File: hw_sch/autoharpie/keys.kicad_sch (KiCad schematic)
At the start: 1 part, among them U5 STM32F030R8Tx

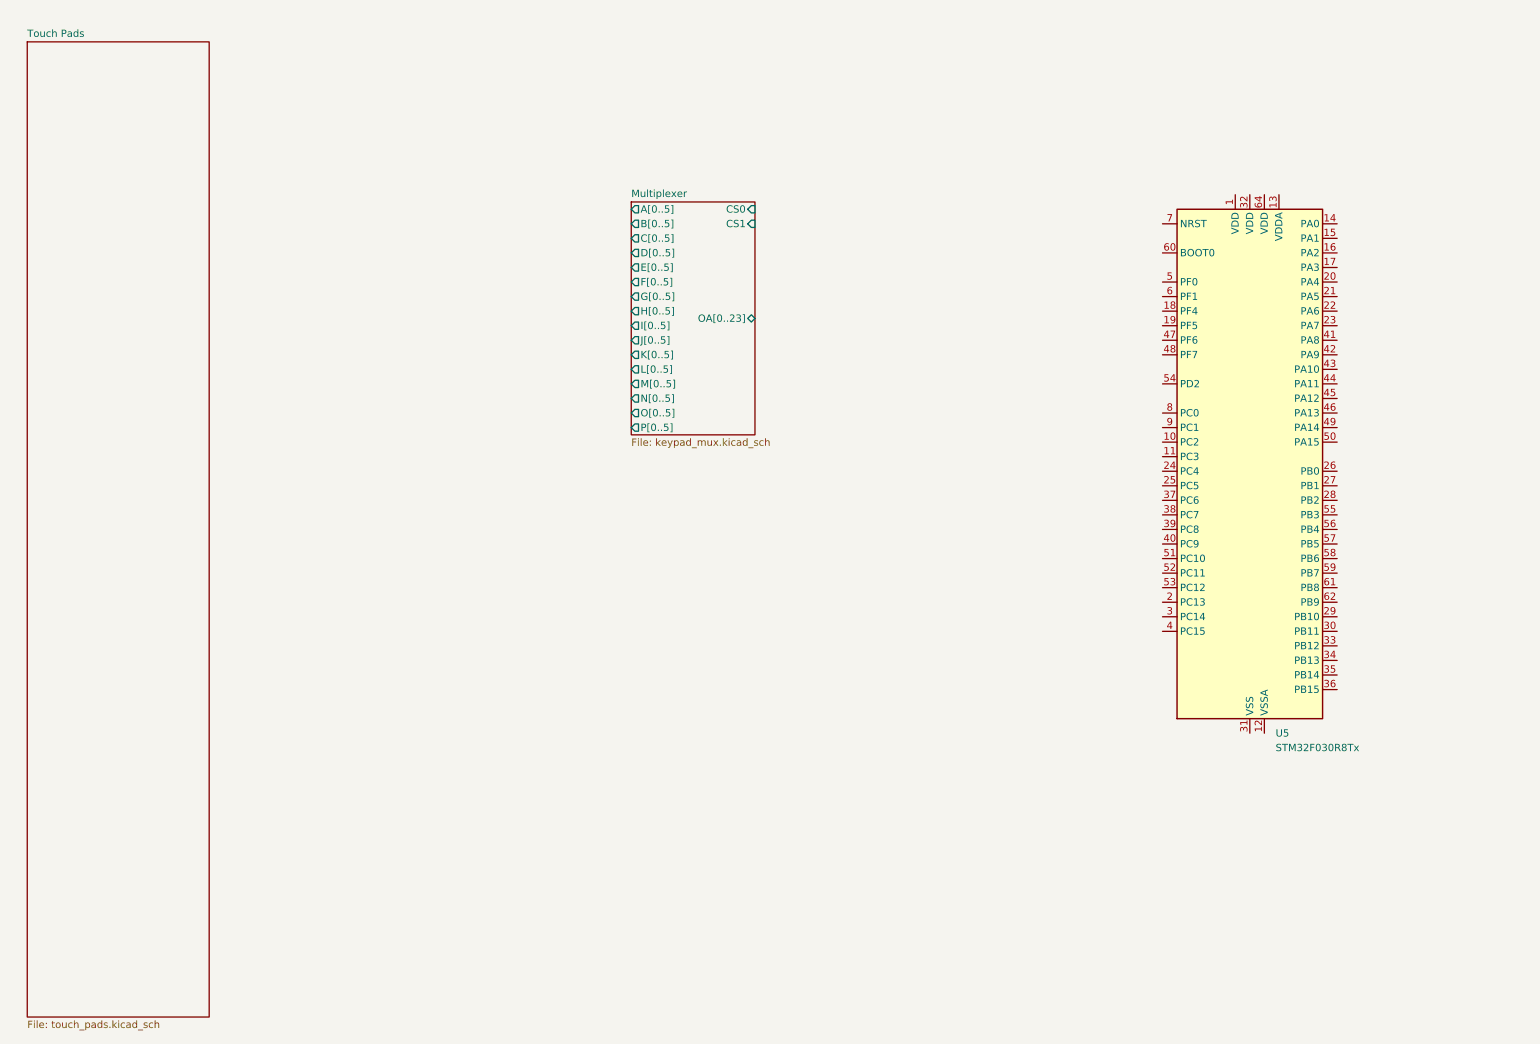
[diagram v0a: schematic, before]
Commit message: switch to teensy reduce pins
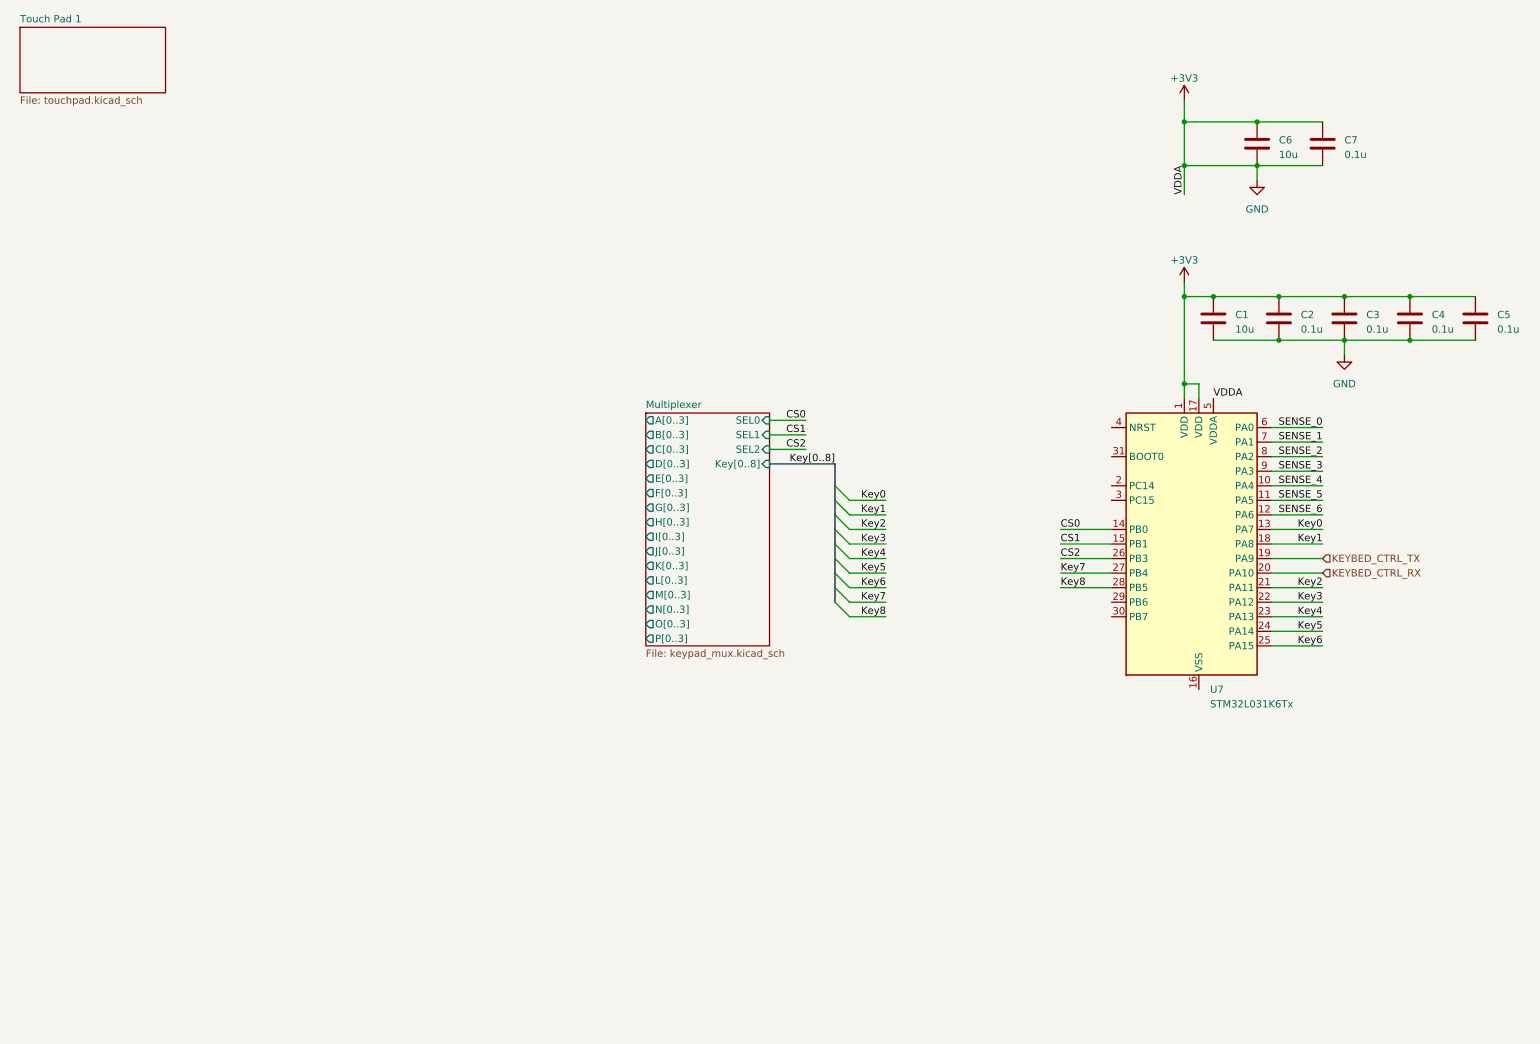
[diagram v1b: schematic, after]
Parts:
- removed U5: STM32F030R8Tx, Package_QFP:LQFP-64_10x10mm_P0.5mm, symbol MCU_ST_STM32F0:STM32F030R8Tx
- added C1, C6: 10u, symbol Device:C
- added C2, C3, C4, C5, C7: 0.1u, symbol Device:C
- added U7: STM32L031K6Tx, Package_QFP:LQFP-32_7x7mm_P0.8mm, symbol MCU_ST_STM32L0:STM32L031K6Tx
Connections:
- new net: U7.16 (VSS), U7.32 (VSS)
- new net +3V3: C1.1, C1.2, C2.1, C2.2, C3.1, C3.2, C4.1, C4.2, C5.1, C5.2, C6.1, C6.2, C7.1, C7.2, U7.1 (VDD), U7.17 (VDD), U7.5 (VDDA)
- new net CS0: U7.14 (PB0)
- new net CS1: U7.15 (PB1)
- new net CS2: U7.26 (PB3)
- new net KEYBED_CTRL_RX: U7.20 (PA10)
- new net KEYBED_CTRL_TX: U7.19 (PA9)
- new net Key0: U7.13 (PA7)
- new net Key1: U7.18 (PA8)
- new net Key2: U7.21 (PA11)
- new net Key3: U7.22 (PA12)
- new net Key4: U7.23 (PA13)
- new net Key5: U7.24 (PA14)
- new net Key6: U7.25 (PA15)
- new net Key7: U7.27 (PB4)
- new net Key8: U7.28 (PB5)
- new net SENSE_0: U7.6 (PA0)
- new net SENSE_1: U7.7 (PA1)
- new net SENSE_2: U7.8 (PA2)
- new net SENSE_3: U7.9 (PA3)
- new net SENSE_4: U7.10 (PA4)
- new net SENSE_5: U7.11 (PA5)
- new net SENSE_6: U7.12 (PA6)
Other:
- removed sheet Touch Pads
- added sheet Touch Pad 1 (touchpad.kicad_sch)
- sheet Multiplexer ports: added A[0..3], B[0..3], C[0..3], D[0..3], E[0..3], F[0..3], G[0..3], H[0..3], I[0..3], J[0..3], K[0..3], Key[0..8], L[0..3], M[0..3], N[0..3], O[0..3], P[0..3], SEL0, SEL1, SEL2; removed A[0..5], B[0..5], CS0, CS1, C[0..5], D[0..5], E[0..5], F[0..5], G[0..5], H[0..5], I[0..5], J[0..5], K[0..5], L[0..5], M[0..5], N[0..5], OA[0..23], O[0..5], P[0..5]

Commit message: matrix, flattening
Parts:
- added C8, C9: 0.1u, symbol Device:C
- added R3: 10k, symbol Device:R
- added TP1, TP10, TP11, TP12, TP13, TP14, TP15, TP16, TP2, TP3, TP4, TP5, TP6, TP7, TP8, TP9: TestPoint, symbol Connector:TestPoint
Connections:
- net CS0 is gone; now on net Key0: U7.14 (PB0)
- net CS1 is gone; now on net Key1: U7.15 (PB1)
- net CS2 is gone; now on net Key2: U7.26 (PB3)
- net SENSE_2 is gone; now on net KEYBED_CTRL_TX: U7.8 (PA2)
- net SENSE_3 is gone; now on net KEYBED_CTRL_RX: U7.9 (PA3)
- net SENSE_5 is gone; now on net Key5: U7.11 (PA5)
- net SENSE_6 is gone; now on net Key6: U7.12 (PA6)
- net +3V3: now also U7.16 (VSS), U7.32 (VSS), C8.2, C9.2, R3.2
- net KEYBED_CTRL_RX: no longer U7.20 (PA10)
- net KEYBED_CTRL_TX: no longer U7.19 (PA9)
- net Key0: now also TP1.1; no longer U7.13 (PA7)
- net Key1: now also TP2.1; no longer U7.18 (PA8)
- net Key2: now also TP3.1; no longer U7.21 (PA11)
- net Key3: now also U7.27 (PB4), TP4.1; no longer U7.22 (PA12)
- net Key4: now also U7.28 (PB5), TP5.1; no longer U7.23 (PA13)
- net Key5: now also TP6.1; no longer U7.24 (PA14)
- net Key6: now also TP7.1; no longer U7.25 (PA15)
- net Key7: now also U7.13 (PA7), TP8.1; no longer U7.27 (PB4)
- net Key8: now also U7.18 (PA8), TP9.1; no longer U7.28 (PB5)
- net KEYPAD_BOOT: now reaches U7.31 (BOOT0)
- net KEYPAD_BOOT: now also C8.1, R3.1
- net KEYPAD_RESET: now reaches U7.4 (NRST)
- net KEYPAD_RESET: now also C9.1
- net SENSE_0: no longer names the net of U7.6 (PA0)
- net SENSE_1: no longer names the net of U7.7 (PA1)
- net SENSE_4: no longer names the net of U7.10 (PA4)
- new net Key10: U7.20 (PA10)
- new net Key11: TP12.1, U7.21 (PA11)
- new net Key12: TP13.1, U7.22 (PA12)
- new net Key13: TP14.1, U7.23 (PA13)
- new net Key14: TP15.1, U7.24 (PA14)
- new net Key15: TP16.1, U7.25 (PA15)
- new net Key9: TP10.1, U7.19 (PA9)
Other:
- removed sheet Multiplexer
- removed sheet Touch Pad 1

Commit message: isolated ground
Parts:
- removed C1, C6: 10u, symbol Device:C
- removed C2, C3, C4, C5, C7, C8, C9: 0.1u, symbol Device:C
- removed R3: 10k, symbol Device:R
- removed TP1, TP10, TP11, TP12, TP13, TP14, TP15, TP16, TP2, TP3, TP4, TP5, TP6, TP7, TP8, TP9: TestPoint, symbol Connector:TestPoint
- removed U7: STM32L031K6Tx, Package_QFP:LQFP-32_7x7mm_P0.8mm, symbol MCU_ST_STM32L0:STM32L031K6Tx
- added U5: FSA3157P6X, Package_TO_SOT_SMD:SOT-363_SC-70-6, symbol Analog_Switch:FSA3157P6X

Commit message: stm32, msp430
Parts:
- removed U5: FSA3157P6X, Package_TO_SOT_SMD:SOT-363_SC-70-6, symbol Analog_Switch:FSA3157P6X
- added C71, C75: 0.1u, symbol Device:C
- added C74: 10u, symbol Device:C
- added C78: 1u, symbol Device:C
- added D26: PMEG2010AEH, Diode_SMD:D_SOD-123F, symbol Diode:PMEG2010AEH
- added J7: Conn_01x10_Socket, Connector_FFC-FPC:Hirose_FH12-35S-0.5SH_1x35-1MP_P0.50mm_Horizontal, symbol Connector:Conn_01x10_Socket
- added J8: Conn_01x04_Pin, symbol Connector:Conn_01x04_Pin
- added J9: Conn_01x10_Pin, symbol Connector:Conn_01x10_Pin
- added R29: 10k, symbol Device:R
- added U8: MSP430FR2633IDAR, DA0032A_N, symbol 2023-03-09_01-52-04:MSP430FR2633IDAR
- added U9: AP2112K-3.3, Package_TO_SOT_SMD:SOT-23-5, symbol Regulator_Linear:AP2112K-3.3
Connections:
- new net: C71.1, D26.1 (K), R29.1, U9.1 (VIN)
- new net 3V3_ISO: C74.1, C75.1, J8.2 (Pin_2), U8.4 (DVCC), U9.5 (VOUT)
- new net 5V_ISO: D26.2 (A), J9.1 (Pin_1)
- new net 5V_ISO_CAP: J7.1 (Pin_1)
- new net CAP_LDO_EN: J7.3 (Pin_3)
- new net GND: C71.2
- new net GND_ISO: C74.2, C75.2, C78.2, J8.1 (Pin_1), J9.2 (Pin_2), U8.3 (DVSS)
- new net GND_ISO_CAP: J7.2 (Pin_2), U9.2 (GND)
- new net PSU_EN: J9.3 (Pin_3), R29.2, U9.3 (EN)
- new net SPY_CLK: J8.3 (Pin_3), U8.6 (TEST_SBWTCK)
- new net SPY_SWD: J8.4 (Pin_4), U8.5 (RST_NMI_SBWTDIO_N)
- new net VREG: C78.1, U8.24 (VREG)
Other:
- added sheet Bus Switch (capsense_bus_switch.kicad_sch)
- added sheet Key Sensor 1 (key_sensor.kicad_sch)

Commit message: DAC, touch sensors
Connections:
- net CAP_SW: now reaches U8.10 (P1-7_UCA0STE_SMCLK_TDO_A7)
- net RX0: now reaches U8.16 (P3-0_CAP0-0)
- net CAP0: now reaches U8.17 (CAP0-1)
- net RX3: now reaches U8.18 (P2-3_CAP0-2)
- net CAP1: now reaches U8.19 (CAP0-3)
- net RX1: now reaches U8.20 (P3-1_UCA1STE_CAP1-0)
- net RX4: now reaches U8.21 (P2-4_UCA1CLK_CAP1-1)
- net RX5: now reaches U8.22 (P2-5_UCA1RXD_UCA1SOMI_CAP1-2)
- net RX6: now reaches U8.23 (P2-6_UCA1TXD_UCA1SIMO_CAP1-3)
- net CAP2: now reaches U8.25 (CAP2-0)
- net CAP3: now reaches U8.26 (CAP2-1)
- net CAP4: now reaches U8.27 (CAP2-2)
- net CAP5: now reaches U8.28 (CAP2-3)
- net RX7: now reaches U8.29 (P2-7_CAP3-0)
- net CAP6: now reaches U8.30 (CAP3-1)
- net RX2: now reaches U8.31 (P3-2_CAP3-2)
- net CAP7: now reaches U8.32 (CAP3-3)
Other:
- added sheet Key Sensor 2 (key_sensor.kicad_sch)
- sheet Bus Switch ports: added SWITCH; removed none
- sheet Key Sensor 1 ports: added I[0..7], RX[0..7]; removed none
- moved on the sheet: U8

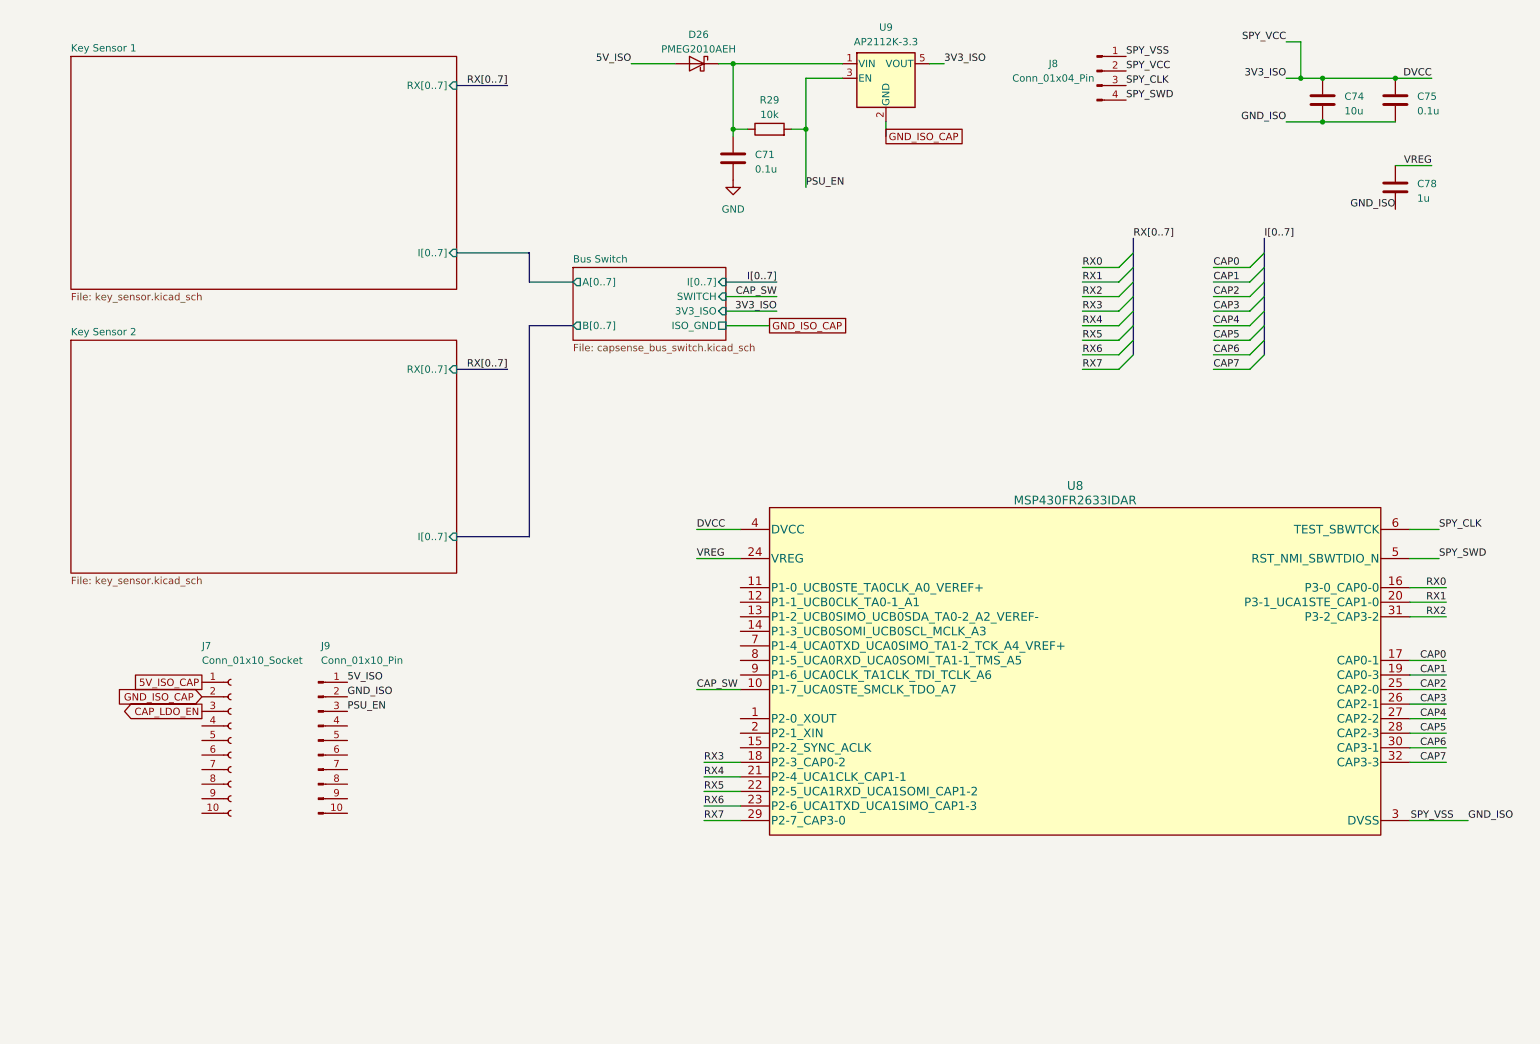
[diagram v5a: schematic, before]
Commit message: DAC wiring, add heirch pins
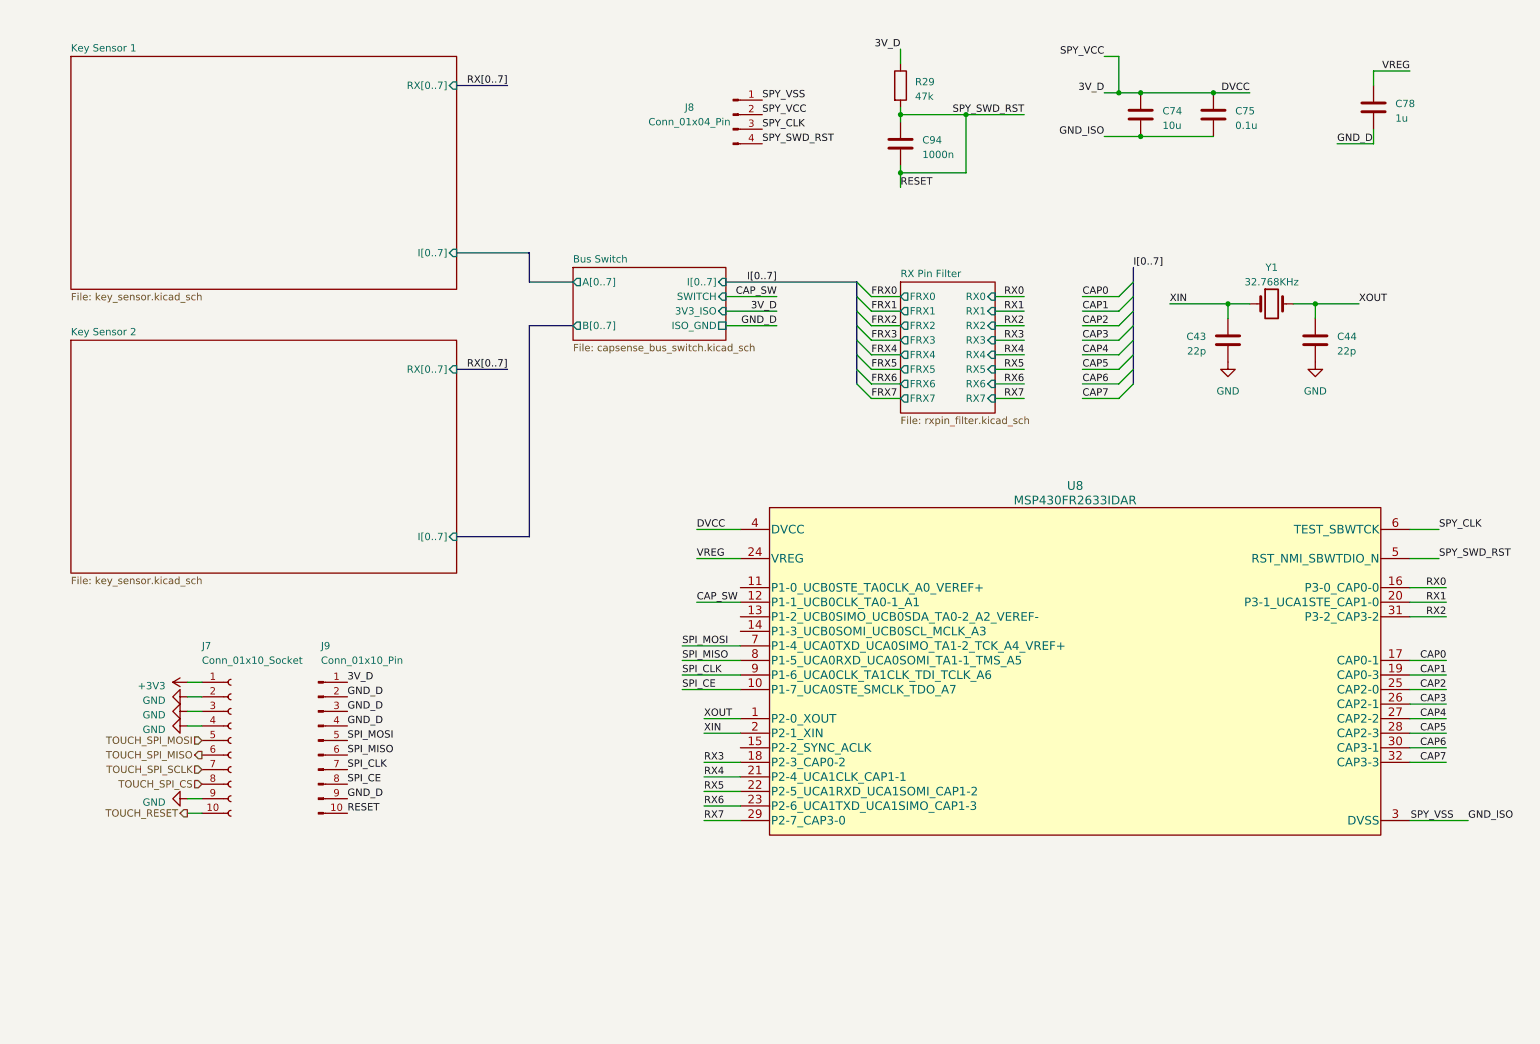
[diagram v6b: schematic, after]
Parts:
- removed C71: 0.1u, symbol Device:C
- removed D26: PMEG2010AEH, Diode_SMD:D_SOD-123F, symbol Diode:PMEG2010AEH
- removed U9: AP2112K-3.3, Package_TO_SOT_SMD:SOT-23-5, symbol Regulator_Linear:AP2112K-3.3
- added C43, C44: 22p, symbol Device:C
- added C94: 1000n, symbol Device:C
- added Y1: 32.768KHz, symbol Device:Crystal
- R29: value 10k -> 47k
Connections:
- net 3V3_ISO is gone; now on net 3V_D: C74.1, C75.1, J8.2 (Pin_2), U8.4 (DVCC)
- net 5V_ISO is gone; now on net 3V_D: J9.1 (Pin_1)
- net CAP_LDO_EN is gone; now on net GND: J7.3 (Pin_3)
- net GND_ISO_CAP is gone; now on net GND: J7.2 (Pin_2)
- net SPY_SWD is gone; now on net RESET: J8.4 (Pin_4), U8.5 (RST_NMI_SBWTDIO_N)
- net CAP_SW: now also U8.12 (P1-1_UCB0CLK_TA0-1_A1); no longer U8.10 (P1-7_UCA0STE_SMCLK_TDO_A7)
- net GND: now also J7.4 (Pin_4), J7.9 (Pin_9), C43.2, C44.2
- net GND_ISO: no longer C78.2, J9.2 (Pin_2)
- net 3V_D: now reaches R29.1
- net XOUT: now reaches U8.1 (P2-0_XOUT)
- net XOUT: now also C44.1, Y1.2
- net XIN: now reaches U8.2 (P2-1_XIN)
- net XIN: now also C43.1, Y1.1
- net SPI_MOSI: now reaches U8.7 (P1-4_UCA0TXD_UCA0SIMO_TA1-2_TCK_A4_VREF+)
- net SPI_MOSI: now also J9.5 (Pin_5)
- net SPI_MISO: now reaches U8.8 (P1-5_UCA0RXD_UCA0SOMI_TA1-1_TMS_A5)
- net SPI_MISO: now also J9.6 (Pin_6)
- net SPI_CLK: now reaches U8.9 (P1-6_UCA0CLK_TA1CLK_TDI_TCLK_A6)
- net SPI_CLK: now also J9.7 (Pin_7)
- net RESET: now reaches J9.10 (Pin_10)
- net RESET: now also R29.2, C94.1, C94.2
- net GND_D: now reaches J9.4 (Pin_4)
- net GND_D: now also C78.2, J9.2 (Pin_2), J9.3 (Pin_3), J9.9 (Pin_9)
- net SPI_CE: now reaches J9.8 (Pin_8)
- net SPI_CE: now also U8.10 (P1-7_UCA0STE_SMCLK_TDO_A7)
- net TOUCH_RESET: now reaches J7.10 (Pin_10)
- net TOUCH_SPI_MOSI: now reaches J7.5 (Pin_5)
- net TOUCH_SPI_MISO: now reaches J7.6 (Pin_6)
- net TOUCH_SPI_SCLK: now reaches J7.7 (Pin_7)
- net TOUCH_SPI_CS: now reaches J7.8 (Pin_8)
- net 5V_ISO_CAP renamed +3V3
- removed net PSU_EN: J9.3 (Pin_3), R29.2
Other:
- added sheet RX Pin Filter (rxpin_filter.kicad_sch)
- moved on the sheet: C74, C75, C78, J8
